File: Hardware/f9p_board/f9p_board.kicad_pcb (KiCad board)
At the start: 2 copper layers, 48 parts, among them J1 USB_B_Mini, J2 USB_B_Mini, J3 GPIO, J4 CAN, J5 Active Antenna, P1 SWD, SW1 F9P_USB_POWER, U1 Ublox_ZED_F9P, U2 STM32F405RGTx, U3 MCP16311MS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

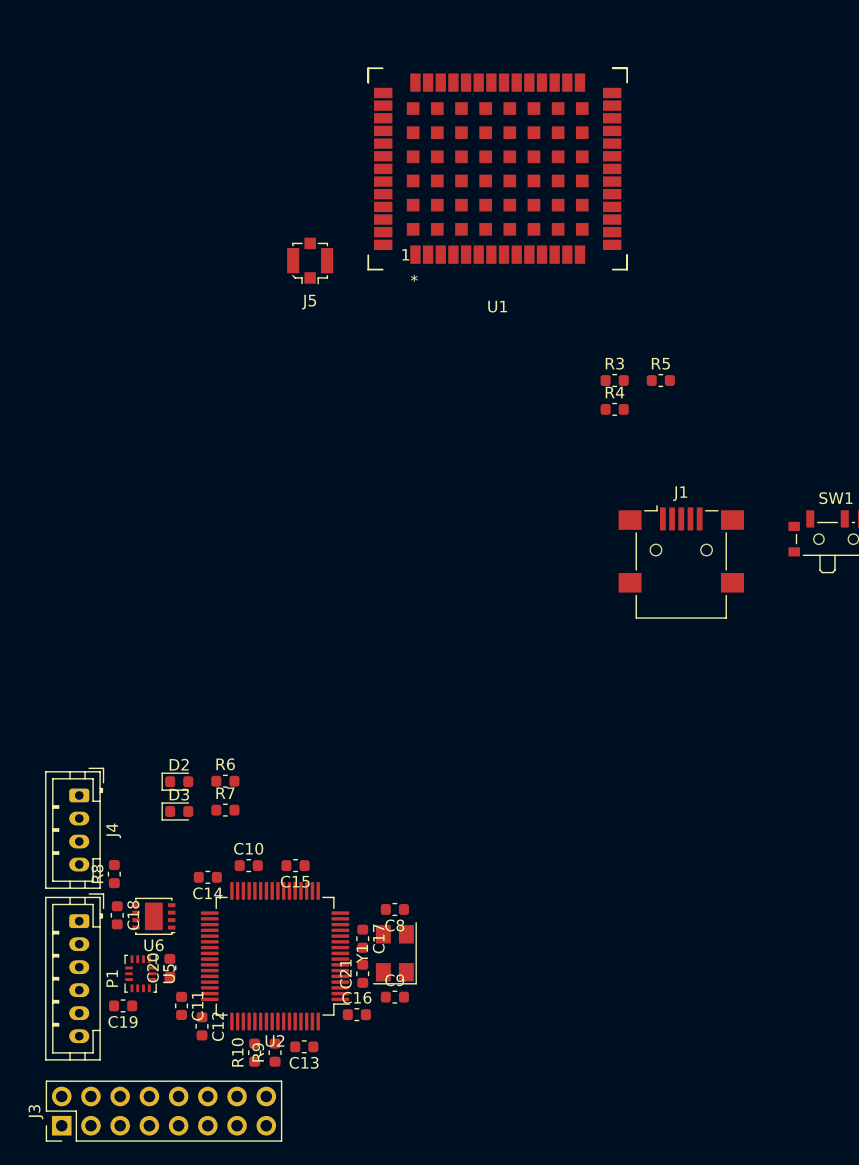
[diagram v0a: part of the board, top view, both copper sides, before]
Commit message: Some more wiring around the F9P and added a library file for the WDFN6 package
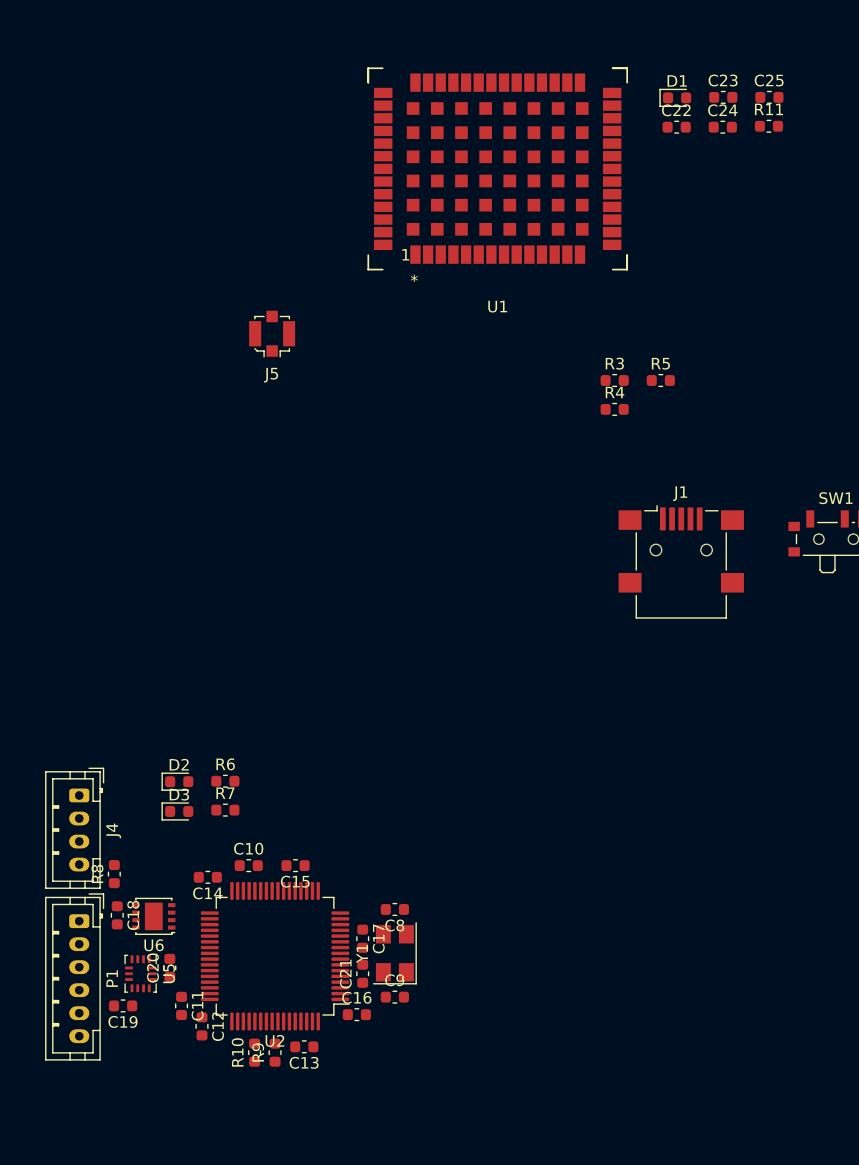
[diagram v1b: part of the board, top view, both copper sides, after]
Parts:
- removed J3: GPIO, Connector_PinHeader_2.54mm:PinHeader_2x08_P2.54mm_Vertical
- added C22: 2.2u, Capacitor_SMD:C_0603_1608Metric, F.Cu at (68.2, 65.4)
- added C23: 2.2u, Capacitor_SMD:C_0603_1608Metric, F.Cu at (72.2, 62.8)
- added C24: 2.2u, Capacitor_SMD:C_0603_1608Metric, F.Cu at (72.2, 65.4)
- added C25: 2.2u, Capacitor_SMD:C_0603_1608Metric, F.Cu at (76.2, 62.8)
- added D1: RED, LED_SMD:LED_0603_1608Metric, F.Cu at (68.2, 62.8)
- added R11: 1k, Resistor_SMD:R_0603_1608Metric, F.Cu at (76.2, 65.3)
- moved J5 7.16 mm to (33.0, 83.3)
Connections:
- net Net-(U1-Pad26) renamed F9P_CORRECTION_RX
- net Net-(U1-Pad27) renamed F9P_CORRECTION_TX
- U1 pad 12: Net-(U1-Pad12) -> GND
- U1 pad 33: Net-(U1-Pad33) -> VCC
- U1 pad 34: Net-(U1-Pad34) -> VCC
- U1 pad 36: Net-(U1-Pad36) -> VCC
- U1 pad 42: Net-(U1-Pad42) -> MCU_RX_F9P_TX
- U1 pad 43: Net-(U1-Pad43) -> MCU_TX_F9P_RX
- U1 pad 49: Net-(U1-Pad49) -> F9P_RESET_N
- U1 pad 53: Net-(U1-Pad53) -> TIMEPULSE
- U1 pad 7: Net-(U1-Pad7) -> VCC
- U2 pad 10: PC2 -> Net-(U2-Pad10)
- U2 pad 11: PC3 -> Net-(U2-Pad11)
- U2 pad 2: PC13 -> Net-(U2-Pad2)
- U2 pad 24: PC4 -> Net-(U2-Pad24)
- U2 pad 25: PC5 -> Net-(U2-Pad25)
- U2 pad 3: PC14 -> Net-(U2-Pad3)
- U2 pad 37: PC6 -> MCU_TX_F9P_RX
- U2 pad 38: PC7 -> MCU_RX_F9P_TX
- U2 pad 39: PC8 -> TIMEPULSE
- U2 pad 4: PC15 -> Net-(U2-Pad4)
- U2 pad 40: PC9 -> F9P_RESET_N
- U2 pad 51: PC10 -> Net-(U2-Pad51)
- U2 pad 52: PC11 -> Net-(U2-Pad52)
- U2 pad 53: PC12 -> Net-(U2-Pad53)
- U2 pad 8: PC0 -> Net-(U2-Pad8)
- U2 pad 9: PC1 -> Net-(U2-Pad9)

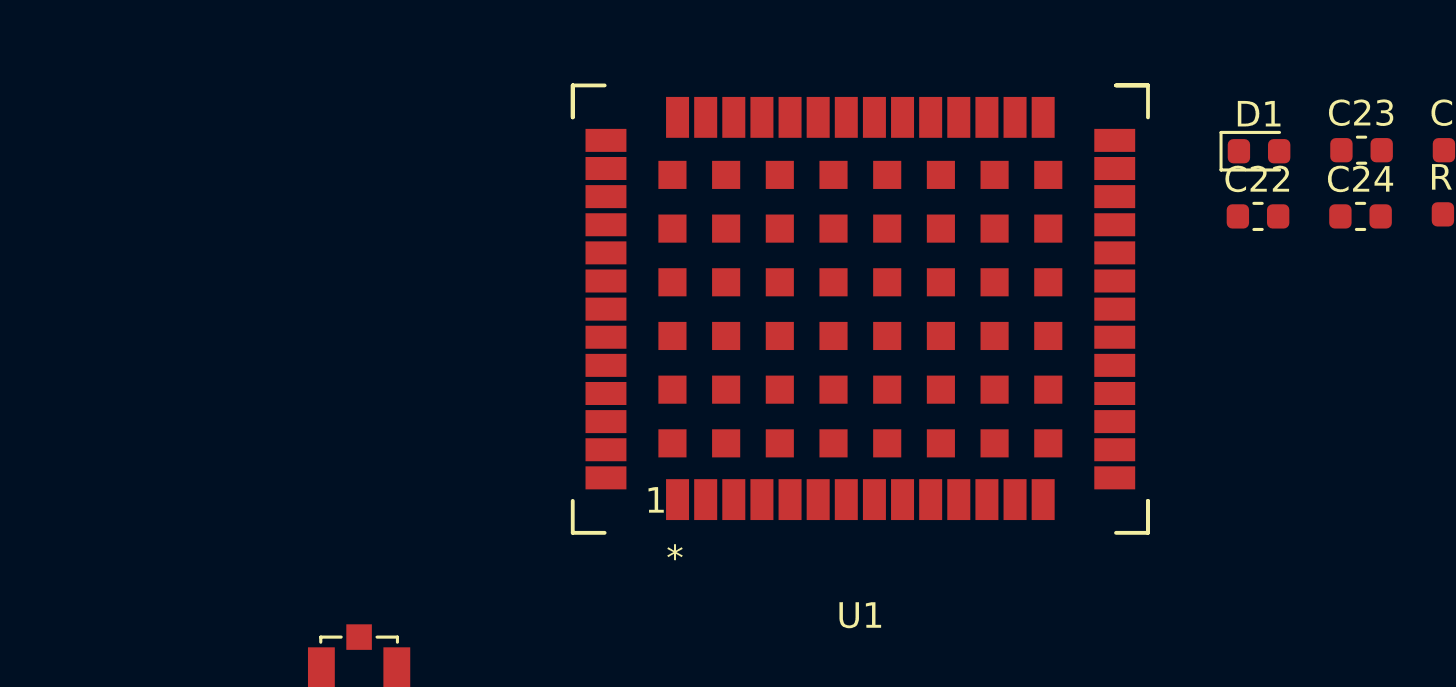
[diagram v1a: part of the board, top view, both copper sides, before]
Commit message: F9P_Board : ERC without complaints. Wiring most things up. Need review
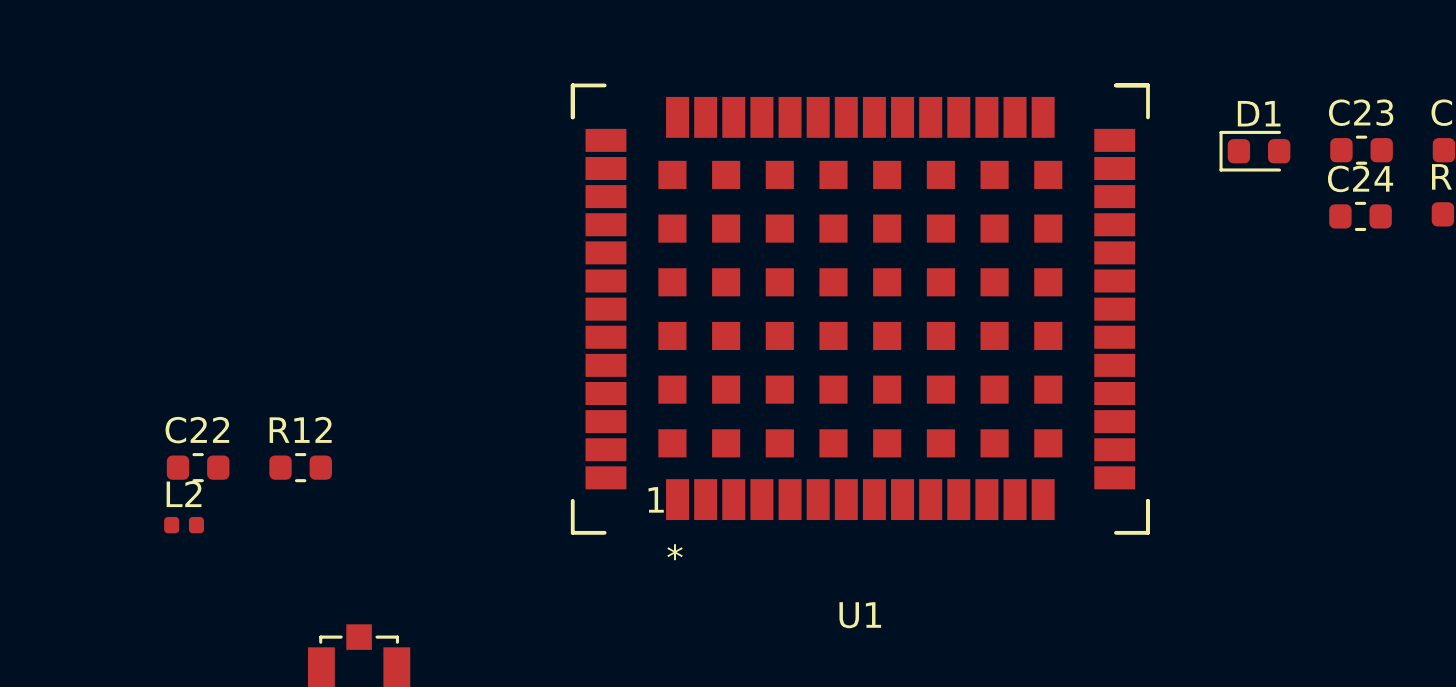
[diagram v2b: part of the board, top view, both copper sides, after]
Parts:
- added L2: 56n, Inductor_SMD:L_0402_1005Metric, F.Cu at (26.2, 77.4)
- added R12: 4.7R, Resistor_SMD:R_0603_1608Metric, F.Cu at (30.7, 75.2)
- C22: value 2.2u -> 100n
- moved C22 42.6 mm to (26.7, 75.2)
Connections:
- C22 pad 1: GND -> Net-(C22-Pad1)
- C22 pad 2: VCC -> GND
- J4 pad 4: CAN_5V -> 5V
- U1 pad 2: Net-(U1-Pad2) -> Net-(J5-Pad1)
- U1 pad 7: VCC -> Net-(R12-Pad1)
- U6 pad 3: CAN_5V -> 5V

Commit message: F9P_Board experimenting with how to lay components out
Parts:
- added J3: GPIO, Connector_PinHeader_2.54mm:PinHeader_2x08_P2.54mm_Vertical, F.Cu at (114.3, 140.2)
- C22, J5, L2, R12, SW1, U1: moved to B.Cu
- moved J2 130.9 mm to (133.1, 138.4), turned to 90 degrees
- moved J4 114.0 mm to (130.0, 116.8), turned to 0 degrees
- moved U3 109.6 mm to (126.2, 137.9), turned to 90 degrees
- moved C4 109.5 mm to (120.7, 141.0), turned to -90 degrees
- moved C2 108.9 mm to (125.2, 143.0), turned to -90 degrees
- moved R2 108.2 mm to (123.4, 143.0), turned to 90 degrees
- moved R1 108.1 mm to (123.4, 139.7), turned to -90 degrees
- moved R8 107.5 mm to (126.0, 117.1)
- moved C1 105.4 mm to (127.0, 143.0), turned to -90 degrees
- moved C5 102.8 mm to (117.9, 140.0), turned to -90 degrees
- moved L1 100.2 mm to (121.4, 135.1), turned to 90 degrees
- moved C6 98.1 mm to (125.5, 131.3)
- moved C3 95.2 mm to (126.2, 133.9)
- moved U4 90.7 mm to (125.5, 129.0)
- moved C7 90.5 mm to (125.5, 126.7)
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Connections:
- net 5V renamed MCU_USB_VBUS
- net F9P_CORRECTION_RX renamed Net-(U1-Pad26)
- net F9P_CORRECTION_TX renamed Net-(U1-Pad27)
- C4 pad 1: MCU_USB_VCC -> VCC
- C5 pad 1: MCU_USB_VCC -> VCC
- L1 pad 1: MCU_USB_VCC -> VCC
- R1 pad 2: MCU_USB_VCC -> VCC
- U1 pad 46: Net-(U1-Pad46) -> TX_READY
- U2 pad 12: Net-(U2-Pad12) -> GND
- U2 pad 14: Net-(U2-Pad14) -> GPIO1
- U2 pad 15: Net-(U2-Pad15) -> GPIO2
- U2 pad 16: Net-(U2-Pad16) -> GPIO3
- U2 pad 17: Net-(U2-Pad17) -> GPIO4
- U2 pad 18: Net-(U2-Pad12) -> GND
- U2 pad 2: Net-(U2-Pad2) -> GPIO10
- U2 pad 20: Net-(U2-Pad20) -> GPIO5
- U2 pad 21: Net-(U2-Pad21) -> GPIO6
- U2 pad 22: Net-(U2-Pad22) -> GPIO7
- U2 pad 23: Net-(U2-Pad23) -> GPIO8
- U2 pad 3: Net-(U2-Pad3) -> GPIO11
- U2 pad 33: Net-(U2-Pad33) -> GPIO13
- U2 pad 34: Net-(U2-Pad34) -> GPIO14
- U2 pad 35: Net-(U2-Pad35) -> GPIO15
- U2 pad 36: Net-(U2-Pad36) -> GPIO16
- U2 pad 4: Net-(U2-Pad4) -> GPIO12
- U2 pad 51: Net-(U2-Pad51) -> TX_READY
- U2 pad 53: Net-(U2-Pad53) -> GPIO9
- U2 pad 63: Net-(U2-Pad63) -> GND

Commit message: experimentation with layout of components
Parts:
- removed J3: GPIO, Connector_PinHeader_2.54mm:PinHeader_2x08_P2.54mm_Vertical
- added H1: MountingHole, MountingHole:MountingHole_3.2mm_M3, F.Cu at (73.5, 63.5)
- added H2: MountingHole, MountingHole:MountingHole_3.2mm_M3, F.Cu at (73.5, 86.5)
- added H3: MountingHole, MountingHole:MountingHole_3.2mm_M3, F.Cu at (116.5, 63.5)
- added H4: MountingHole, MountingHole:MountingHole_3.2mm_M3, F.Cu at (116.5, 86.5)
- C11, C21, C23, C24, C25, C6, C7, D1, R11, R3, R8, U4: moved to B.Cu
- C22, J5, R12: moved to F.Cu
- L2: footprint Inductor_SMD:L_0402_1005Metric -> Inductor_SMD:L_0603_1608Metric; moved to F.Cu
- moved C12 114.7 mm to (107.3, 66.0), turned to 180 degrees
- moved C18 112.3 mm to (107.0, 63.5)
- moved U6 112.2 mm to (110.0, 63.5)
- moved R12 111.3 mm to (88.7, 64.8), turned to 90 degrees
- moved C22 110.1 mm to (90.3, 64.8)
- moved C14 106.0 mm to (113.2, 70.9), turned to -90 degrees
- moved C11 105.7 mm to (108.0, 77.4), turned to 180 degrees
- moved L2 105.4 mm to (87.0, 64.8), turned to 90 degrees
- moved J5 102.1 mm to (83.4, 65.5), turned to 90 degrees
- moved C9 98.5 mm to (104.2, 63.3), turned to 90 degrees
- moved C13 97.1 mm to (97.8, 70.7), turned to 90 degrees
- moved C21 96.6 mm to (108.3, 69.8), turned to 180 degrees
- moved C19 96.0 mm to (84.5, 70.5), turned to -90 degrees
- moved U5 94.4 mm to (86.7, 70.5)
- moved C15 93.4 mm to (103.5, 66.0), turned to 0 degrees
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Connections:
- U1 pad 46: TX_READY -> Net-(U1-Pad46)
- U2 pad 14: GPIO1 -> Net-(U2-Pad14)
- U2 pad 15: GPIO2 -> Net-(U2-Pad15)
- U2 pad 16: GPIO3 -> Net-(U2-Pad16)
- U2 pad 17: GPIO4 -> Net-(U2-Pad17)
- U2 pad 2: GPIO10 -> Net-(U2-Pad2)
- U2 pad 20: GPIO5 -> Net-(U2-Pad20)
- U2 pad 21: GPIO6 -> Net-(U2-Pad21)
- U2 pad 22: GPIO7 -> Net-(U2-Pad22)
- U2 pad 23: GPIO8 -> Net-(U2-Pad23)
- U2 pad 3: GPIO11 -> Net-(U2-Pad3)
- U2 pad 33: GPIO13 -> Net-(U2-Pad33)
- U2 pad 34: GPIO14 -> Net-(U2-Pad34)
- U2 pad 35: GPIO15 -> Net-(U2-Pad35)
- U2 pad 36: GPIO16 -> Net-(U2-Pad36)
- U2 pad 4: GPIO12 -> Net-(U2-Pad4)
- U2 pad 51: TX_READY -> Net-(U2-Pad51)
- U2 pad 53: GPIO9 -> Net-(U2-Pad53)
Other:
- board outline added: 50 x 30 mm
- rule trace_min: 0.2 -> 0.18

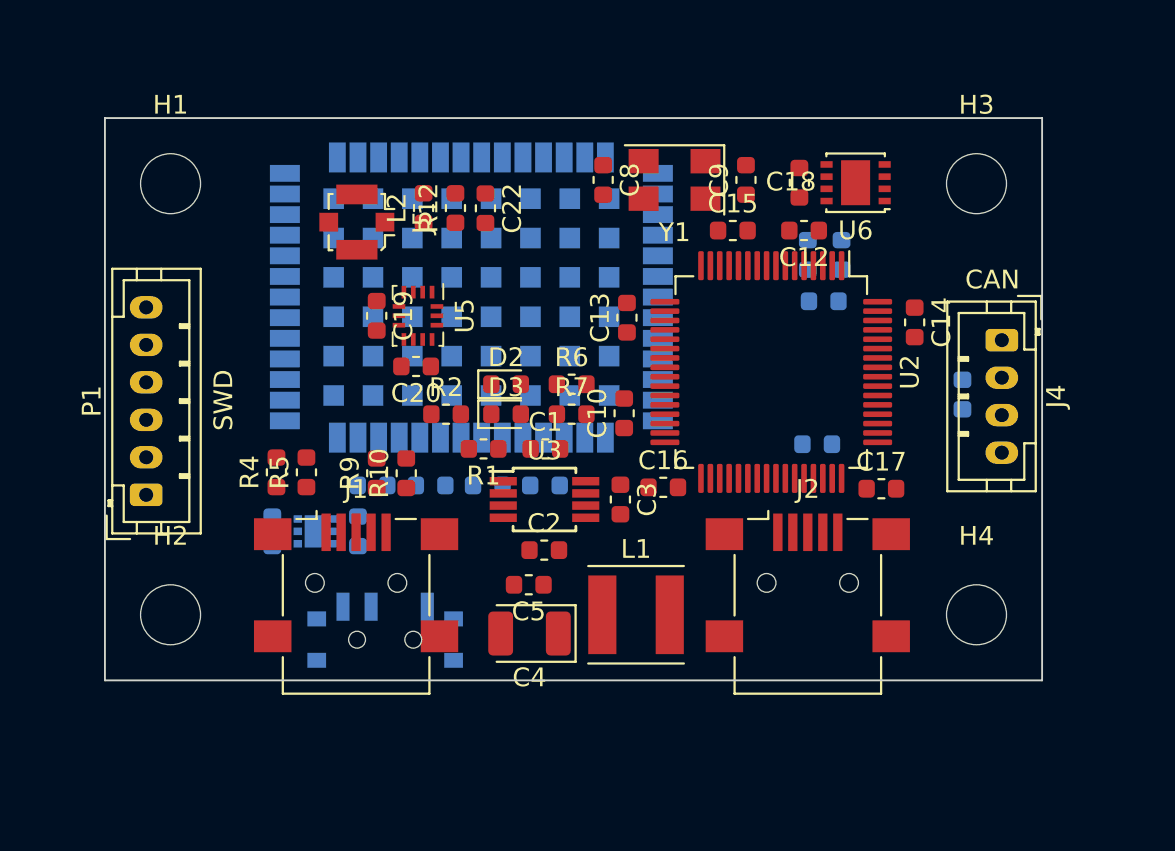
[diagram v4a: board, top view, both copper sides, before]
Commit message: f9p_board: started to route and some some small rearrangements
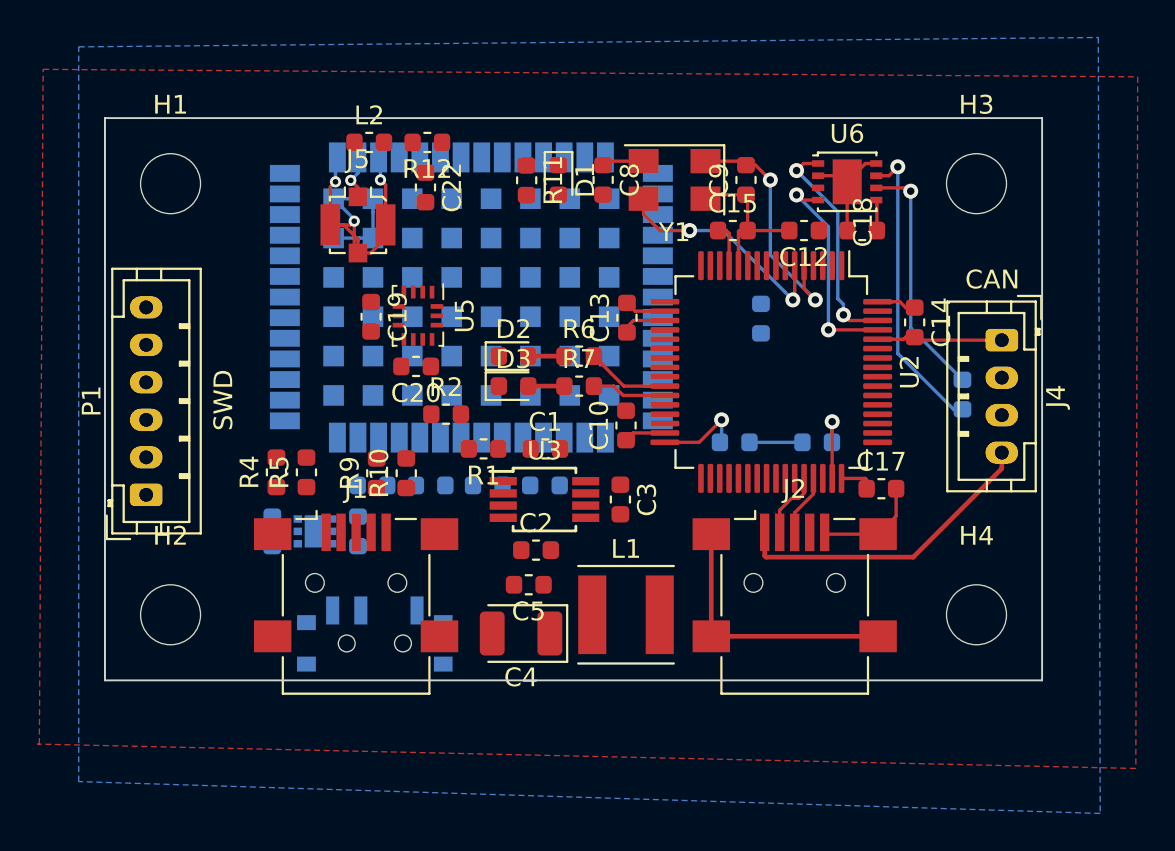
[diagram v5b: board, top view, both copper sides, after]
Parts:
- C16: moved to B.Cu
- D1, R11: moved to F.Cu
- moved R11 17.3 mm to (92.5, 63.3)
- moved D1 13.9 mm to (94.2, 63.3)
- moved L2 4.55 mm to (84.1, 61.3), turned to 0 degrees
- moved C16 4.51 mm to (103.6, 77.3)
- moved C18 4.21 mm to (110.4, 66.0), turned to 180 degrees
- moved R12 3.81 mm to (87.2, 61.3), turned to 180 degrees
- moved C21 3.48 mm to (105.0, 70.7), turned to 90 degrees
- moved C22 3.39 mm to (87.1, 63.7)
- moved D2 1.55 mm to (91.8, 72.7)
- moved D3 1.55 mm to (91.8, 74.3)
- moved R6 1.55 mm to (95.3, 72.7)
- moved R7 1.55 mm to (95.3, 74.3)
- moved J2 0.70 mm to (106.8, 84.8)
- moved C10 0.66 mm to (97.8, 76.4)
- moved SW1 0.59 mm to (84.4, 87.7)
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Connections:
- J5 pad 2: (no net) -> GND
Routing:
- net GND: track 0.00 -> 74.8 mm, vias 0 -> 3
- net MCU_USB_VBUS: track 0.00 -> 16.7 mm
- net CANH: track 0.00 -> 16.0 mm, vias 0 -> 1
- net VCC: track 0.00 -> 15.2 mm, vias 0 -> 1
- net Net-(C9-Pad2): track 0.00 -> 13.3 mm, vias 0 -> 2
- net CANL: track 0.00 -> 13.1 mm, vias 0 -> 1
- net Net-(C8-Pad2): track 0.00 -> 12.5 mm, vias 0 -> 2
- net CAN_TX: track 0.00 -> 12.0 mm, vias 0 -> 2
- net CAN_RX: track 0.00 -> 11.8 mm, vias 0 -> 2
- net Net-(R6-Pad2): track 0.00 -> 4.45 mm
- net Net-(C11-Pad1): track 0.00 -> 4.13 mm, vias 0 -> 1
- net Net-(R7-Pad2): track 0.00 -> 3.99 mm
- net MCU_USB_DM: track 0.00 -> 3.65 mm
- net MCU_USB_DP: track 0.00 -> 3.29 mm
- net Net-(J5-Pad1): track 0.00 -> 2.42 mm, vias 0 -> 1
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- added copper zone on B.Cu, net GND
- added copper zone on F.Cu, net GND
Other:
- rule solder_mask_min_width: 0.25 -> 0.025
- rule via_min_size: 0.4 -> 0.3
